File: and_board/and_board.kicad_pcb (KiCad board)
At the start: 2 copper layers, 52.1 x 27.9 mm, 12 parts, among them J1 SJ1-2503A, J2 SJ1-2503A, J3 SJ1-2503A, U1 SN74LS08N

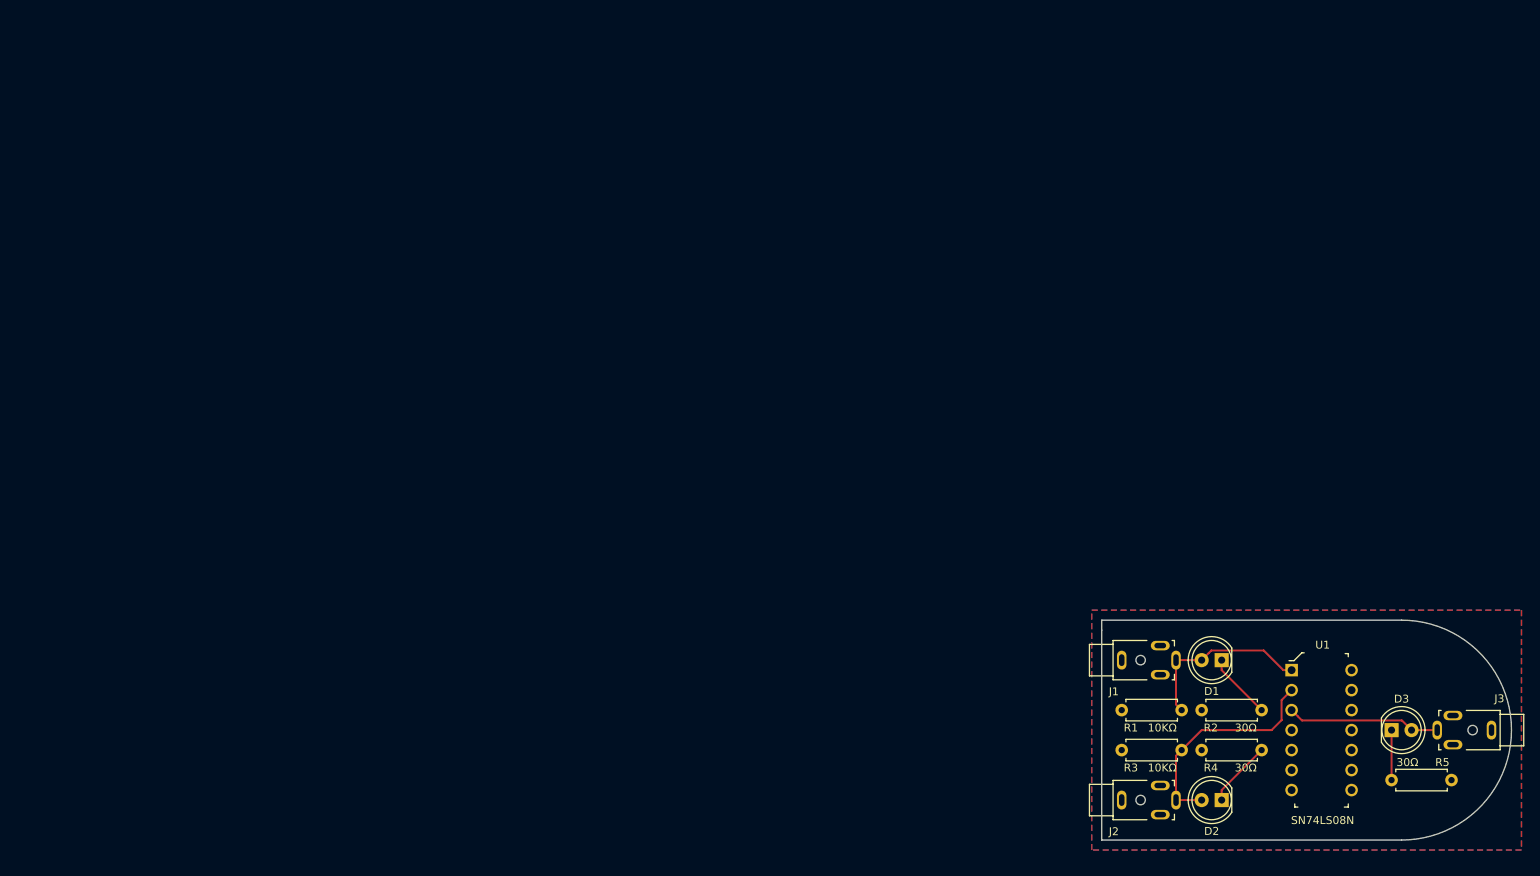
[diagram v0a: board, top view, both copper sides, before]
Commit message: Updated outline for 'and' board
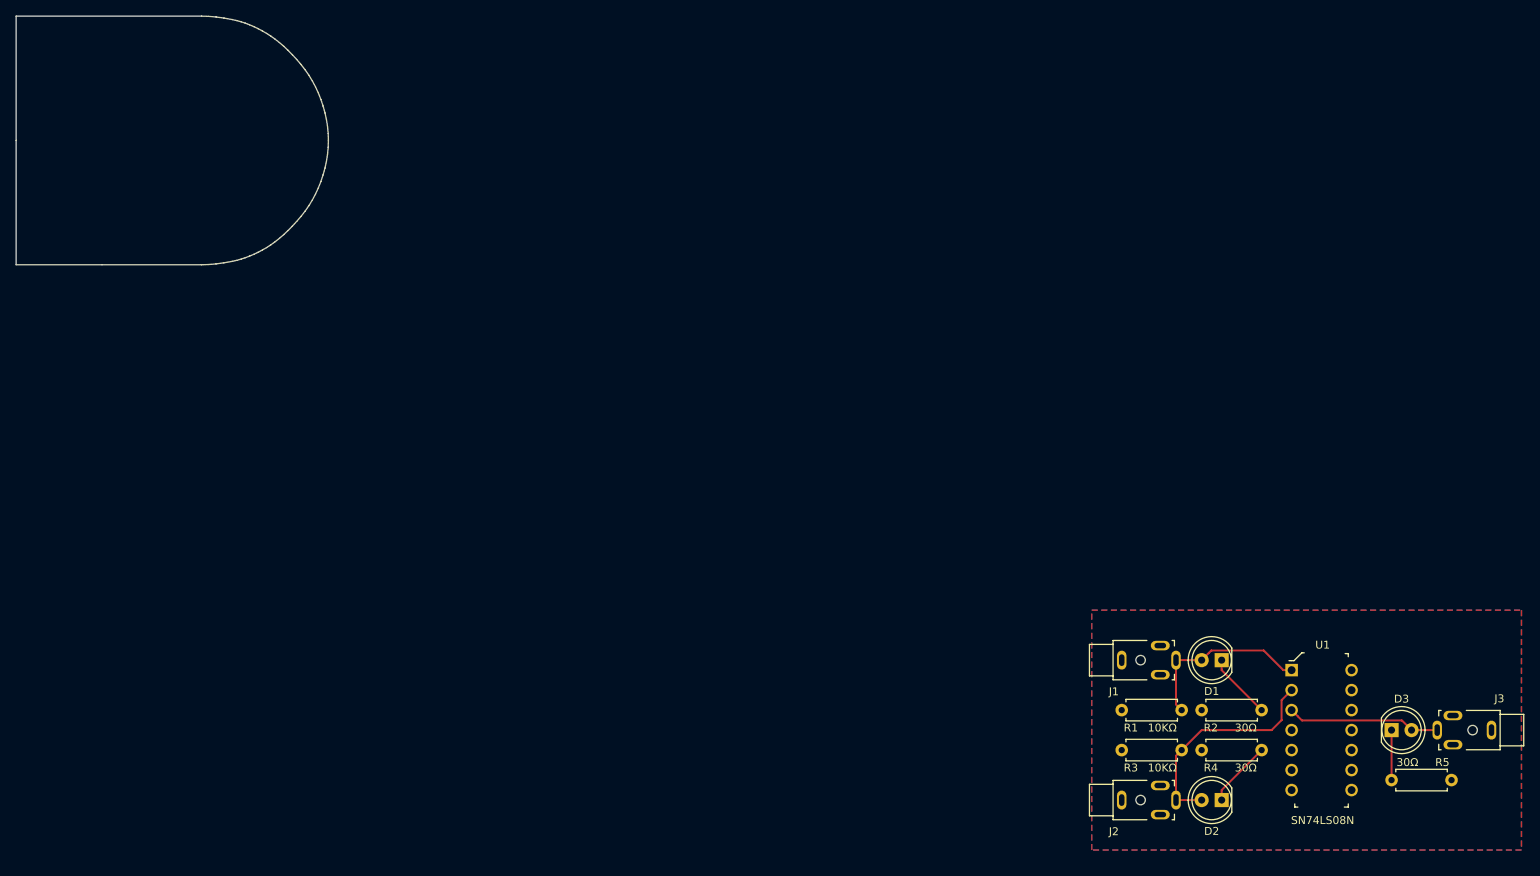
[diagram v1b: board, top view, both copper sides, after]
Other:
- board size 52.1 x 27.9 mm -> 39.7 x 31.6 mm
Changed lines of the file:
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@@
   (general
     (thickness 1.6)
-    (drawings 5)
+    (drawings 0)
     (tracks 26)
     (zones 0)
@@
   (page A4)
   (layers
-    (0 F.Cu signal)
-    (31 B.Cu signal)
-    (32 B.Adhes user)
-    (33 F.Adhes user)
-    (34 B.Paste user)
-    (35 F.Paste user)
-    (36 B.SilkS user)
-    (37 F.SilkS user)
-    (38 B.Mask user)
-    (39 F.Mask user)
-    (40 Dwgs.User user)
-    (41 Cmts.User user)
-    (42 Eco1.User user)
-    (43 Eco2.User user)
+    (0 F.Cu signal hide)
+    (31 B.Cu signal hide)
+    (32 B.Adhes user hide)
+    (33 F.Adhes user hide)
+    (34 B.Paste user hide)
+    (35 F.Paste user hide)
+    (36 B.SilkS user hide)
+    (37 F.SilkS user hide)
+    (38 B.Mask user hide)
+    (39 F.Mask user hide)
+    (40 Dwgs.User user hide)
+    (41 Cmts.User user hide)
+    (42 Eco1.User user hide)
+    (43 Eco2.User user hide)
     (44 Edge.Cuts user)
-    (45 Margin user)
-    (46 B.CrtYd user)
-    (47 F.CrtYd user)
-    (48 B.Fab user)
+    (45 Margin user hide)
+    (46 B.CrtYd user hide)
+    (47 F.CrtYd user hide)
+    (48 B.Fab user hide)
     (49 F.Fab user hide)
   )
@@
     (solder_mask_min_width 0.25)
     (aux_axis_origin 0 0)
-    (visible_elements FFFFFF7F)
+    (visible_elements 7FFFFFFF)
     (pcbplotparams
       (layerselection 0x010fc_ffffffff)
@@
     )
   )
-  (gr_line (start 118.11 88.9) (end 156.21 88.9) (layer Edge.Cuts) (width 0.05))
-  (gr_line (start 156.21 60.96) (end 118.11 60.96) (layer Edge.Cuts) (width 0.05))
-  (gr_arc (start 156.21 74.93) (end 156.21 88.9) (angle -180) (layer Edge.Cuts) (width 0.05))
-  (gr_line (start 118.11 60.96) (end 118.11 62.23) (layer Edge.Cuts) (width 0.05))
-  (gr_line (start 118.11 62.23) (end 118.11 88.9) (layer Edge.Cuts) (width 0.05))
   (segment (start 131.709999 65.140001) (end 130.81 66.04) (width 0.25) (layer F.Cu) (net 1))
   (segment (start 138.694999 64.814999) (end 132.035001 64.814999) (width 0.25) (layer F.Cu) (net 1))
@@
     (connect_pads (clearance 0.508))
     (min_thickness 0.254)
-    (fill yes (arc_segments 32) (thermal_gap 0.508) (thermal_bridge_width 0.508))
+    (fill (arc_segments 32) (thermal_gap 0.508) (thermal_bridge_width 0.508))
     (polygon
       (pts
@@
     (connect_pads (clearance 0.508))
     (min_thickness 0.254)
-    (fill yes (arc_segments 32) (thermal_gap 0.508) (thermal_bridge_width 0.508))
+    (fill (arc_segments 32) (thermal_gap 0.508) (thermal_bridge_width 0.508))
     (polygon
       (pts
@@
     )
   )
+  (gr_line (start -19.840528 -15.797023) (end 3.714584 -15.797023) (layer Edge.Cuts) (width 0.1))
+  (gr_line (start 3.714584 -15.797023) (end 4.614384 -15.769574) (layer Edge.Cuts) (width 0.1))
+  (gr_line (start 4.614384 -15.769574) (end 5.568647 -15.687228) (layer Edge.Cuts) (width 0.1))
+  (gr_line (start 5.568647 -15.687228) (end 6.577300 -15.549987) (layer Edge.Cuts) (width 0.1))
+  (gr_line (start 6.577300 -15.549987) (end 7.640273 -15.357850) (layer Edge.Cuts) (width 0.1))
+  (gr_line (start 7.640273 -15.357850) (end 8.185555 -15.234332) (layer Edge.Cuts) (width 0.1))
+  (gr_line (start 8.185555 -15.234332) (end 8.730632 -15.083367) (layer Edge.Cuts) (width 0.1))
+  (gr_line (start 8.730632 -15.083367) (end 9.275370 -14.904953) (layer Edge.Cuts) (width 0.1))
+  (gr_line (start 9.275370 -14.904953) (end 9.819634 -14.699090) (layer Edge.Cuts) (width 0.1))
+  (gr_line (start 9.819634 -14.699090) (end 10.363292 -14.465776) (layer Edge.Cuts) (width 0.1))
+  (gr_line (start 10.363292 -14.465776) (end 10.906209 -14.205010) (layer Edge.Cuts) (width 0.1))
+  (gr_line (start 10.906209 -14.205010) (end 11.448252 -13.916791) (layer Edge.Cuts) (width 0.1))
+  (gr_line (start 11.448252 -13.916791) (end 11.989286 -13.601117) (layer Edge.Cuts) (width 0.1))
+  (gr_line (start 11.989286 -13.601117) (end 12.534594 -13.254988) (layer Edge.Cuts) (width 0.1))
+  (gr_line (start 12.534594 -13.254988) (end 13.079848 -12.865816) (layer Edge.Cuts) (width 0.1))
+  (gr_line (start 13.079848 -12.865816) (end 13.625067 -12.434227) (layer Edge.Cuts) (width 0.1))
+  (gr_line (start 13.625067 -12.434227) (end 14.170267 -11.960842) (layer Edge.Cuts) (width 0.1))
+  (gr_line (start 14.170267 -11.960842) (end 14.715468 -11.446285) (layer Edge.Cuts) (width 0.1))
+  (gr_line (start 14.715468 -11.446285) (end 15.260685 -10.891180) (layer Edge.Cuts) (width 0.1))
+  (gr_line (start 15.260685 -10.891180) (end 15.805939 -10.296150) (layer Edge.Cuts) (width 0.1))
+  (gr_line (start 15.805939 -10.296150) (end 16.351245 -9.661818) (layer Edge.Cuts) (width 0.1))
+  (gr_line (start 16.351245 -9.661818) (end 16.876133 -8.988798) (layer Edge.Cuts) (width 0.1))
+  (gr_line (start 16.876133 -8.988798) (end 17.360111 -8.287544) (layer Edge.Cuts) (width 0.1))
+  (gr_line (start 17.360111 -8.287544) (end 17.803170 -7.558524) (layer Edge.Cuts) (width 0.1))
+  (gr_line (start 17.803170 -7.558524) (end 18.205302 -6.802208) (layer Edge.Cuts) (width 0.1))
+  (gr_line (start 18.205302 -6.802208) (end 18.566499 -6.019065) (layer Edge.Cuts) (width 0.1))
+  (gr_line (start 18.566499 -6.019065) (end 18.886750 -5.209564) (layer Edge.Cuts) (width 0.1))
+  (gr_line (start 18.886750 -5.209564) (end 19.166049 -4.374172) (layer Edge.Cuts) (width 0.1))
+  (gr_line (start 19.166049 -4.374172) (end 19.404385 -3.513360) (layer Edge.Cuts) (width 0.1))
+  (gr_line (start 19.404385 -3.513360) (end 19.595226 -2.635018) (layer Edge.Cuts) (width 0.1))
+  (gr_line (start 19.595226 -2.635018) (end 19.731541 -1.756670) (layer Edge.Cuts) (width 0.1))
+  (gr_line (start 19.731541 -1.756670) (end 19.813330 -0.878318) (layer Edge.Cuts) (width 0.1))
+  (gr_line (start 19.813330 -0.878318) (end 19.840592 0.000035) (layer Edge.Cuts) (width 0.1))
+  (gr_line (start 19.840592 0.000035) (end 19.813330 0.878388) (layer Edge.Cuts) (width 0.1))
+  (gr_line (start 19.813330 0.878388) (end 19.731541 1.756740) (layer Edge.Cuts) (width 0.1))
+  (gr_line (start 19.731541 1.756740) (end 19.595226 2.635087) (layer Edge.Cuts) (width 0.1))
+  (gr_line (start 19.595226 2.635087) (end 19.404385 3.513430) (layer Edge.Cuts) (width 0.1))
+  (gr_line (start 19.404385 3.513430) (end 19.165825 4.378046) (layer Edge.Cuts) (width 0.1))
+  (gr_line (start 19.165825 4.378046) (end 18.886361 5.215216) (layer Edge.Cuts) (width 0.1))
+  (gr_line (start 18.886361 5.215216) (end 18.566004 6.024942) (layer Edge.Cuts) (width 0.1))
+  (gr_line (start 18.566004 6.024942) (end 18.204766 6.807222) (layer Edge.Cuts) (width 0.1))
+  (gr_line (start 18.204766 6.807222) (end 17.802660 7.562057) (layer Edge.Cuts) (width 0.1))
+  (gr_line (start 17.802660 7.562057) (end 17.359696 8.289446) (layer Edge.Cuts) (width 0.1))
+  (gr_line (start 17.359696 8.289446) (end 16.875887 8.989390) (layer Edge.Cuts) (width 0.1))
+  (gr_line (start 16.875887 8.989390) (end 16.351245 9.661888) (layer Edge.Cuts) (width 0.1))
+  (gr_line (start 16.351245 9.661888) (end 15.805939 10.295698) (layer Edge.Cuts) (width 0.1))
+  (gr_line (start 15.805939 10.295698) (end 15.260685 10.889580) (layer Edge.Cuts) (width 0.1))
+  (gr_line (start 15.260685 10.889580) (end 14.715468 11.443536) (layer Edge.Cuts) (width 0.1))
+  (gr_line (start 14.715468 11.443536) (end 14.170267 11.957566) (layer Edge.Cuts) (width 0.1))
+  (gr_line (start 14.170267 11.957566) (end 13.625067 12.431671) (layer Edge.Cuts) (width 0.1))
+  (gr_line (start 13.625067 12.431671) (end 13.079848 12.865852) (layer Edge.Cuts) (width 0.1))
+  (gr_line (start 13.079848 12.865852) (end 12.534594 13.260110) (layer Edge.Cuts) (width 0.1))
+  (gr_line (start 12.534594 13.260110) (end 11.989286 13.614446) (layer Edge.Cuts) (width 0.1))
+  (gr_line (start 11.989286 13.614446) (end 11.448469 13.925720) (layer Edge.Cuts) (width 0.1))
+  (gr_line (start 11.448469 13.925720) (end 10.906529 14.210635) (layer Edge.Cuts) (width 0.1))
+  (gr_line (start 10.906529 14.210635) (end 10.363625 14.469035) (layer Edge.Cuts) (width 0.1))
+  (gr_line (start 10.363625 14.469035) (end 9.819918 14.700764) (layer Edge.Cuts) (width 0.1))
+  (gr_line (start 9.819918 14.700764) (end 9.275570 14.905666) (layer Edge.Cuts) (width 0.1))
+  (gr_line (start 9.275570 14.905666) (end 8.730739 15.083584) (layer Edge.Cuts) (width 0.1))
+  (gr_line (start 8.730739 15.083584) (end 8.185586 15.234362) (layer Edge.Cuts) (width 0.1))
+  (gr_line (start 8.185586 15.234362) (end 7.640273 15.357843) (layer Edge.Cuts) (width 0.1))
+  (gr_line (start 7.640273 15.357843) (end 6.576978 15.549983) (layer Edge.Cuts) (width 0.1))
+  (gr_line (start 6.576978 15.549983) (end 5.568361 15.687227) (layer Edge.Cuts) (width 0.1))
+  (gr_line (start 5.568361 15.687227) (end 4.614277 15.769574) (layer Edge.Cuts) (width 0.1))
+  (gr_line (start 4.614277 15.769574) (end 3.714584 15.797023) (layer Edge.Cuts) (width 0.1))
+  (gr_line (start 3.714584 15.797023) (end -8.935401 15.797023) (layer Edge.Cuts) (width 0.1))
+  (gr_line (start -8.935401 15.797023) (end -19.840528 15.797023) (layer Edge.Cuts) (width 0.1))
+  (gr_line (start -19.840528 15.797023) (end -19.840528 -0.013265) (layer Edge.Cuts) (width 0.1))
+  (gr_line (start -19.840528 -0.013265) (end -19.840528 -15.797023) (layer Edge.Cuts) (width 0.1))
+  (gr_line (start -19.840528 -15.797023) (end -19.840528 -15.797023) (layer Edge.Cuts) (width 0.1))
 )

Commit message: Changed outline for 'and' board
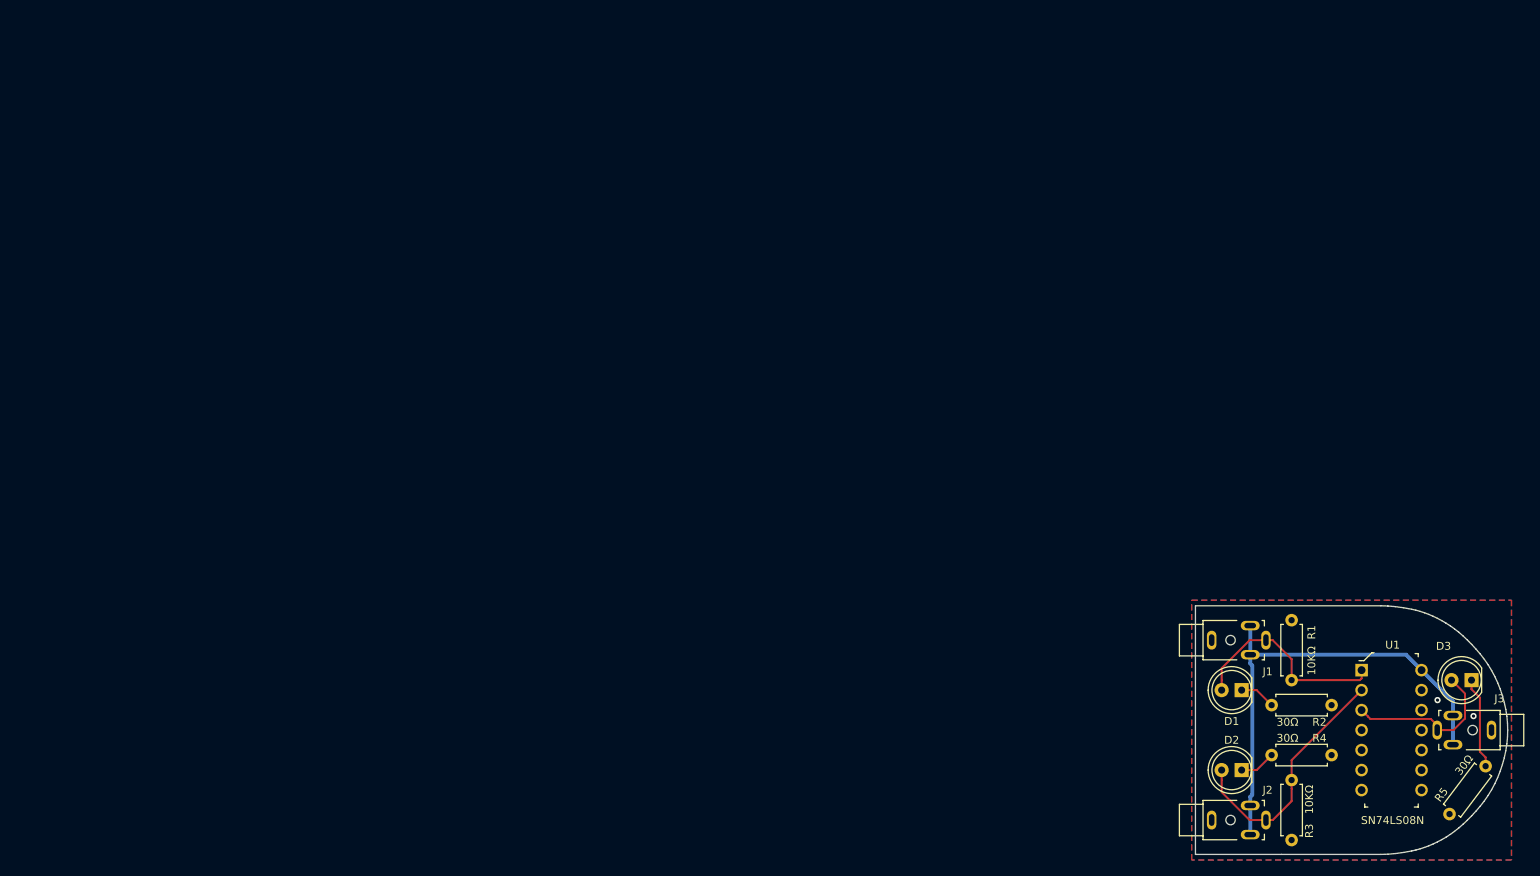
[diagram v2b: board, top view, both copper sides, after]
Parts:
- moved R3 24.4 mm to (142.2, 88.9), turned to 90 degrees
- moved R1 24.4 mm to (142.2, 61.0), turned to 270 degrees
- moved R2 16.5 mm to (147.3, 71.8), turned to 180 degrees
- moved R4 16.5 mm to (147.3, 78.1), turned to 180 degrees
- moved D3 12.0 mm to (165.1, 68.6), turned to 180 degrees
- moved J1 11.7 mm to (132.1, 63.5)
- moved J2 11.7 mm to (132.1, 86.4)
- moved U1 8.89 mm to (151.1, 67.3)
- moved D1 4.58 mm to (135.9, 69.8)
- moved D2 4.58 mm to (135.9, 80.0)
- moved R5 4.33 mm to (162.3, 85.6), turned to 53 degrees
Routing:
- net +5V: track 0.00 -> 60.5 mm
- net Net-(D3-Pad1): track 6.35 -> 11.7 mm
- net Net-(D1-Pad2): track 22.9 -> 26.9 mm
- net Net-(D2-Pad1): track 8.45 -> 4.60 mm
- net Net-(D1-Pad1): track 8.45 -> 4.60 mm
- net Net-(D2-Pad2): track 28.5 -> 31.9 mm
- net Net-(D3-Pad2): track 19.6 -> 20.8 mm
- net GND: vias 0 -> 2
- added copper zone on B.Cu, net GND
- removed copper zone on B.Cu, net +5V

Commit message: PCB tweaks
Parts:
- moved R1 1.27 mm to (143.5, 61.0)
- moved R3 1.27 mm to (143.5, 88.9)
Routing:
- net Net-(D1-Pad2): track 26.9 -> 25.6 mm
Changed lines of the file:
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@@
     (thickness 1.6)
     (drawings 70)
-    (tracks 53)
+    (tracks 52)
     (zones 0)
     (modules 12)
@@
   )
   (setup
-    (last_trace_width 0.5)
+    (last_trace_width 0.25)
     (user_trace_width 0.5)
     (trace_clearance 0.2)
@@
   )
   (module conduWIT_parts:R_Axial_DIN0207_L6.3mm_D2.5mm_P7.62mm_Horizontal (layer F.Cu)
-    (at 142.24 88.9 90)
+    (at 143.51 88.9 90)
     (descr "Resistor, Axial_DIN0207 series, Axial, Horizontal, pin pitch=7.62mm, 0.25W = 1/4W, length*diameter=6.3*2.5mm^2, http://cdn-reichelt.de/documents/datenblatt/B400/1_4W%23YAG.pdf")
     (tags "Resistor Axial_DIN0207 series Axial Horizontal pin pitch 7.62mm 0.25W = 1/4W length 6.3mm diameter 2.5mm")
@@
   )
   (module conduWIT_parts:R_Axial_DIN0207_L6.3mm_D2.5mm_P7.62mm_Horizontal (layer F.Cu)
-    (at 142.24 60.96 270)
+    (at 143.51 60.96 270)
     (descr "Resistor, Axial_DIN0207 series, Axial, Horizontal, pin pitch=7.62mm, 0.25W = 1/4W, length*diameter=6.3*2.5mm^2, http://cdn-reichelt.de/documents/datenblatt/B400/1_4W%23YAG.pdf")
     (tags "Resistor Axial_DIN0207 series Axial Horizontal pin pitch 7.62mm 0.25W = 1/4W length 6.3mm diameter 2.5mm")
@@
   (segment (start 136.912182 63.5) (end 133.35 67.062182) (width 0.25) (layer F.Cu) (net 1))
   (segment (start 138.98 63.5) (end 136.912182 63.5) (width 0.25) (layer F.Cu) (net 1))
+  (segment (start 138.98 64.05) (end 138.98 63.5) (width 0.25) (layer F.Cu) (net 1))
+  (segment (start 143.51 68.58) (end 138.98 64.05) (width 0.25) (layer F.Cu) (net 1))
   (segment (start 151.13 68.36) (end 151.13 67.31) (width 0.25) (layer F.Cu) (net 1))
   (segment (start 150.91 68.58) (end 151.13 68.36) (width 0.25) (layer F.Cu) (net 1))
-  (segment (start 142.24 68.58) (end 150.91 68.58) (width 0.25) (layer F.Cu) (net 1))
-  (segment (start 139.834 63.5) (end 138.98 63.5) (width 0.25) (layer F.Cu) (net 1))
-  (segment (start 142.24 65.906) (end 139.834 63.5) (width 0.25) (layer F.Cu) (net 1))
-  (segment (start 142.24 68.58) (end 142.24 65.906) (width 0.25) (layer F.Cu) (net 1))
+  (segment (start 143.51 68.58) (end 150.91 68.58) (width 0.25) (layer F.Cu) (net 1))
   (segment (start 137.795 69.85) (end 139.7 71.755) (width 0.25) (layer F.Cu) (net 2))
   (segment (start 135.89 69.85) (end 137.795 69.85) (width 0.25) (layer F.Cu) (net 2))
@@
   (segment (start 136.912182 86.36) (end 133.35 82.797818) (width 0.25) (layer F.Cu) (net 3))
   (segment (start 138.98 86.36) (end 136.912182 86.36) (width 0.25) (layer F.Cu) (net 3))
-  (segment (start 142.24 82.41137) (end 142.24 81.28) (width 0.25) (layer F.Cu) (net 3))
-  (segment (start 142.24 83.954) (end 142.24 82.41137) (width 0.25) (layer F.Cu) (net 3))
-  (segment (start 139.834 86.36) (end 142.24 83.954) (width 0.25) (layer F.Cu) (net 3))
+  (segment (start 143.51 82.684) (end 143.51 82.41137) (width 0.25) (layer F.Cu) (net 3))
+  (segment (start 143.51 82.41137) (end 143.51 81.28) (width 0.25) (layer F.Cu) (net 3))
+  (segment (start 139.834 86.36) (end 143.51 82.684) (width 0.25) (layer F.Cu) (net 3))
   (segment (start 138.98 86.36) (end 139.834 86.36) (width 0.25) (layer F.Cu) (net 3))
-  (segment (start 142.24 78.74) (end 151.13 69.85) (width 0.25) (layer F.Cu) (net 3))
-  (segment (start 142.24 81.28) (end 142.24 78.74) (width 0.25) (layer F.Cu) (net 3))
+  (segment (start 143.51 77.47) (end 151.13 69.85) (width 0.25) (layer F.Cu) (net 3))
+  (segment (start 143.51 81.28) (end 143.51 77.47) (width 0.25) (layer F.Cu) (net 3))
   (segment (start 137.795 80.01) (end 139.7 78.105) (width 0.25) (layer F.Cu) (net 4))
   (segment (start 135.89 80.01) (end 137.795 80.01) (width 0.25) (layer F.Cu) (net 4))
